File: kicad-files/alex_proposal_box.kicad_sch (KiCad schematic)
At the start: 40 parts, among them J1 Conn_01x06_Pin, J2 Conn_01x06_Socket, Q1 2N7000, Q10 2N7000, Q11 2N7000, Q2 2N7000, Q3 2N7000, Q4 2N7000, Q5 2N7000, Q6 2N7000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

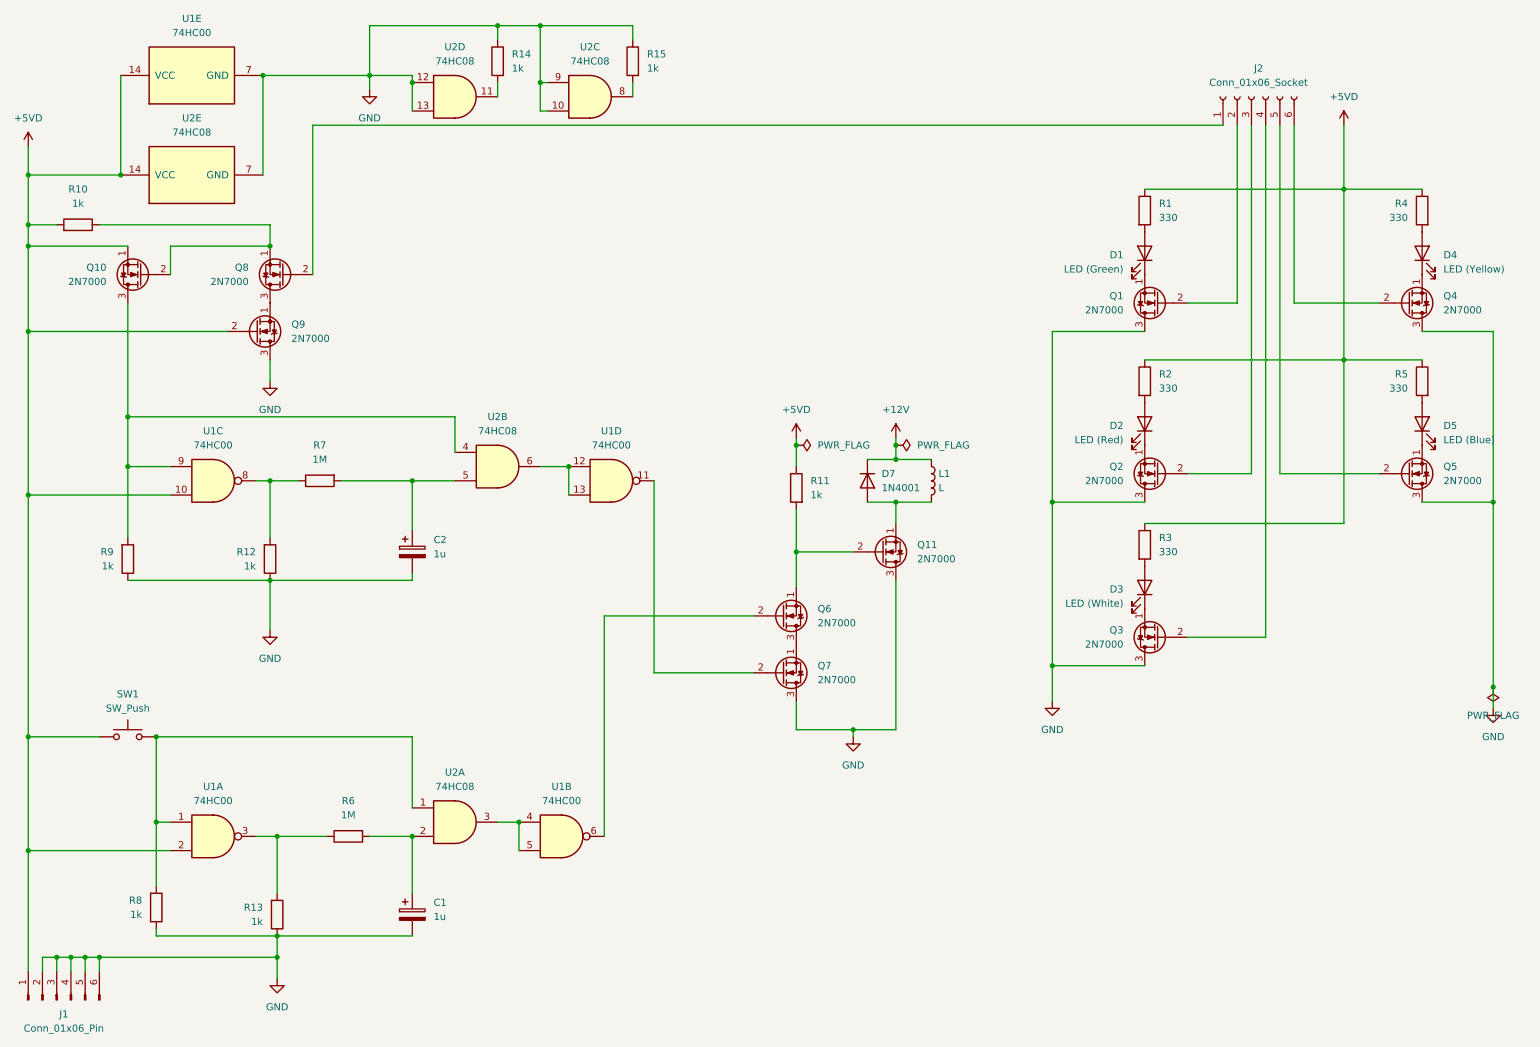
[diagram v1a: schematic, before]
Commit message: made the schematic printable on a PCB
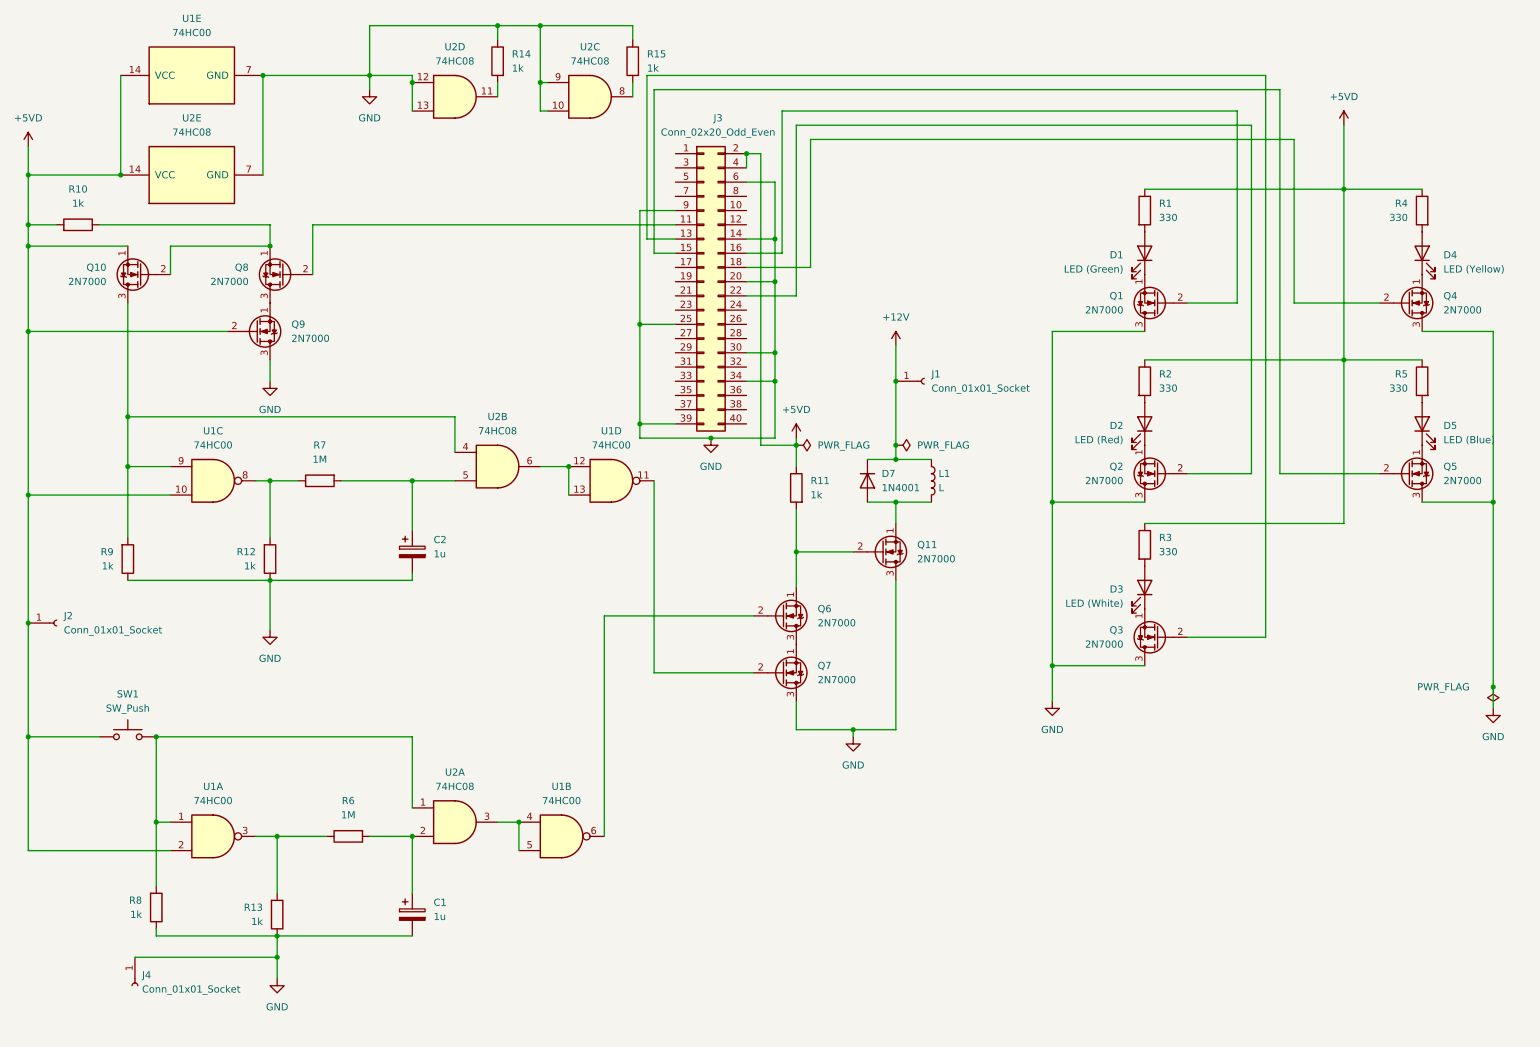
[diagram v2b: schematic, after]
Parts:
- removed J1: Conn_01x06_Pin, Connector_PinHeader_2.00mm:PinHeader_1x06_P2.00mm_Vertical, symbol Connector:Conn_01x06_Pin
- removed J2: Conn_01x06_Socket, Connector_PinSocket_1.00mm:PinSocket_1x06_P1.00mm_Vertical, symbol Connector:Conn_01x06_Socket
- added J1, J2, J4: Conn_01x01_Socket, Connector_PinSocket_2.00mm:PinSocket_1x01_P2.00mm_Vertical, symbol Connector:Conn_01x01_Socket
- added J3: Conn_02x20_Odd_Even, Connector_PinHeader_2.54mm:PinHeader_2x20_P2.54mm_Vertical, symbol Connector_Generic:Conn_02x20_Odd_Even
- C1, C2: footprint Capacitor_THT:CP_Axial_L10.0mm_D4.5mm_P15.00mm_Horizontal -> Capacitor_THT:CP_Radial_D5.0mm_P2.50mm
- D1, D2, D3, D4, D5: footprint Diode_THT:D_5KPW_P7.62mm_Vertical_AnodeUp -> Diode_THT:D_DO-15_P2.54mm_Vertical_AnodeUp
- R1, R10, R11, R12, R13, R14, R15, R2, R3, R4, R5, R6, R7, R8, R9: footprint Resistor_THT:R_Axial_DIN0204_L3.6mm_D1.6mm_P1.90mm_Vertical -> Resistor_THT:R_Axial_DIN0411_L9.9mm_D3.6mm_P12.70mm_Horizontal
- SW1: footprint Button_Switch_THT:Push_E-Switch_KS01Q01 -> SamsFootprints:SW_PUSH-6.5mm
- U1, U2: footprint Package_DIP:SMDIP-14_W7.62mm -> Package_DIP:DIP-14_W7.62mm_Socket_LongPads
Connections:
- net +12V: now also J1.1 (Pin_1)
- net +5VD: now also J2.1 (Pin_1), J3.2 (Pin_2), J3.4 (Pin_4)
- net GND: now also J3.14 (Pin_14), J3.20 (Pin_20), J3.25 (Pin_25), J3.30 (Pin_30), J3.34 (Pin_34), J3.39 (Pin_39), J3.6 (Pin_6), J3.9 (Pin_9), J4.1 (Pin_1)
- net at Q3.2 (G): now also J3.13 (Pin_13)
- net at Q1.2 (G): now also J3.16 (Pin_16)
- net at Q8.2 (G): now also J3.11 (Pin_11)
- net at Q4.2 (G): now also J3.18 (Pin_18)
- net at Q2.2 (G): now also J3.22 (Pin_22)
- net at Q5.2 (G): now also J3.15 (Pin_15)
